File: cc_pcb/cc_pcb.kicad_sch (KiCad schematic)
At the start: 93 parts, among them J1 Conn_02x05_Odd_Even, J2 Micro_SD_Card_Det_Hirose_DM3AT, J3 4x4 Keypad, J4 DC-DC_JUMPER, J5 PS_WIRES, J6 PS_BJ, J7 DC-DC Converter, SW1 SW_Push, U1 ESP8266, U2 7in_display_controller, U3 RFID_Scanner, U4 TFT_2.8IN_DISPLAY, U5 74HC14, U6 STM32F091RCTx, U7 LD1117S33TR_SOT223, U8 TPS56325x, U9 4N28

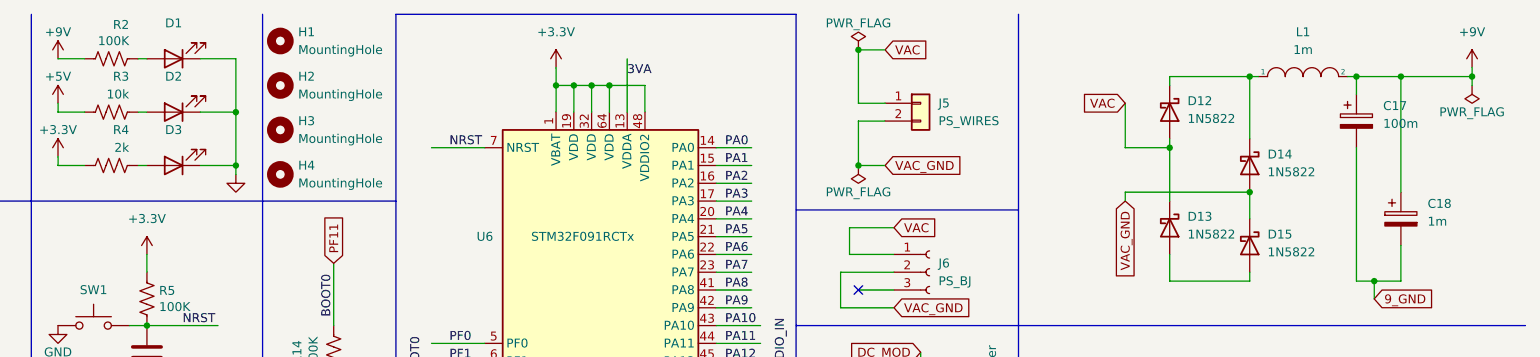
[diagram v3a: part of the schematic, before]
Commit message: 1:1 footprint changes and layout modded to follow rules
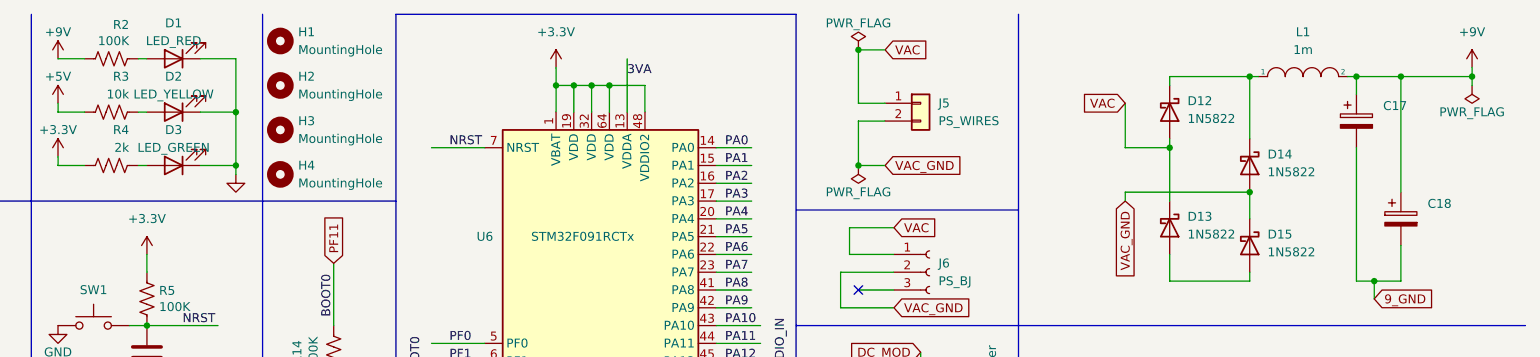
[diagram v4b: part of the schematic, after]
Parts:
- C17: value 100m -> (none); footprint Capacitor_THT:CP_Radial_D8.0mm_P3.50mm -> (none)
- C18: value 1m -> (none)
- D1: value (none) -> LED_RED
- D2: value (none) -> LED_YELLOW
- D3: value (none) -> LED_GREEN
- H1, H2: footprint (none) -> MountingHole:MountingHole_8.4mm_M8
- H5, H9: footprint (none) -> MountingHole:MountingHole_2.2mm_M2_ISO7380
- L2: footprint Inductor_THT:L_Radial_D7.5mm_P5.00mm_Fastron_07P -> (none)
- U2: footprint (none) -> imported_footprints:RA8875_TFT_Breakout
- U8: footprint (none) -> Package_TO_SOT_SMD:SOT-563
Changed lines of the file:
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@@
   (junction (at 74.93 146.05) (diameter 0) (color 0 0 0 0)
   )
-  (junction (at 147.32 184.15) (diameter 0) (color 0 0 0 0)
-  )
   (junction (at 262.89 100.33) (diameter 0) (color 0 0 0 0)
   )
@@
   (junction (at 135.89 156.21) (diameter 0) (color 0 0 0 0)
   )
+  (junction (at 147.32 184.15) (diameter 0) (color 0 0 0 0)
+  )
   (junction (at 215.9 154.94) (diameter 0) (color 0 0 0 0)
   )
@@
     (stroke (width 0) (type default) (color 0 0 0 0))
   )
-  (wire (pts (xy 147.32 184.15) (xy 154.94 184.15))
-    (stroke (width 0) (type default) (color 0 0 0 0))
-  )
   (wire (pts (xy 264.16 86.36) (xy 264.16 78.74))
     (stroke (width 0) (type default) (color 0 0 0 0))
@@
     (stroke (width 0) (type default) (color 0 0 0 0))
   )
+  (wire (pts (xy 147.32 184.15) (xy 154.94 184.15))
+    (stroke (width 0) (type default) (color 0 0 0 0))
+  )
   (wire (pts (xy 160.02 173.99) (xy 160.02 184.15))
     (stroke (width 0) (type default) (color 0 0 0 0))
@@
       (effects (font (size 1.27 1.27)) (justify left))
     )
-    (property "Footprint" "" (id 2) (at 106.68 22.86 0)
+    (property "Footprint" "MountingHole:MountingHole_8.4mm_M8" (id 2) (at 106.68 22.86 0)
       (effects (font (size 1.27 1.27)) hide)
     )
@@
       (effects (font (size 1.27 1.27)) (justify left))
     )
-    (property "Footprint" "" (id 2) (at 35.56 171.45 0)
+    (property "Footprint" "imported_footprints:RA8875_TFT_Breakout" (id 2) (at 35.56 171.45 0)
       (effects (font (size 1.27 1.27)) hide)
     )
@@
       (effects (font (size 1.27 1.27)) (justify left))
     )
-    (property "Footprint" "" (id 2) (at 182.88 77.47 0)
+    (property "Footprint" "MountingHole:MountingHole_2.2mm_M2_ISO7380" (id 2) (at 182.88 77.47 0)
       (effects (font (size 1.27 1.27)) hide)
     )
@@
     (property "Reference" "L2" (id 0) (at 271.78 77.47 0))
     (property "Value" "2.2uH" (id 1) (at 271.78 74.93 0))
-    (property "Footprint" "Inductor_THT:L_Radial_D7.5mm_P5.00mm_Fastron_07P" (id 2) (at 271.78 73.66 0)
+    (property "Footprint" "" (id 2) (at 271.78 73.66 0)
       (effects (font (size 1.27 1.27)) hide)
     )
@@
     (pin "1")
   )
-  (symbol (lib_id "power:+3.3V") (at 154.94 184.15 0) (unit 1)
-    (in_bom yes) (on_board yes) (fields_autoplaced)
-    (property "Reference" "#PWR024" (id 0) (at 154.94 187.96 0)
-      (effects (font (size 1.27 1.27)) hide)
-    )
-    (property "Value" "+3.3V" (id 1) (at 154.94 179.07 0))
-    (property "Footprint" "" (id 2) (at 154.94 184.15 0)
-      (effects (font (size 1.27 1.27)) hide)
-    )
-    (property "Datasheet" "" (id 3) (at 154.94 184.15 0)
-      (effects (font (size 1.27 1.27)) hide)
-    )
-    (pin "1")
-  )
   (symbol (lib_id "Mechanical:MountingHole") (at 15.24 125.73 0) (unit 1)
     (in_bom yes) (on_board yes) (fields_autoplaced)
@@
       (effects (font (size 1.27 1.27)) (justify left))
     )
-    (property "Footprint" "" (id 2) (at 15.24 125.73 0)
+    (property "Footprint" "MountingHole:MountingHole_2.2mm_M2_ISO7380" (id 2) (at 15.24 125.73 0)
       (effects (font (size 1.27 1.27)) hide)
     )
@@
       (effects (font (size 1.27 1.27)) (justify left))
     )
-    (property "Value" "100m" (id 1) (at 264.16 28.3209 0)
+    (property "Value" "" (id 1) (at 264.16 28.3209 0)
       (effects (font (size 1.27 1.27)) (justify left))
     )
-    (property "Footprint" "Capacitor_THT:CP_Radial_D8.0mm_P3.50mm" (id 2) (at 261.3152 31.75 0)
+    (property "Footprint" "" (id 2) (at 261.3152 31.75 0)
       (effects (font (size 1.27 1.27)) hide)
     )
@@
     (in_bom yes) (on_board yes)
     (property "Reference" "D1" (id 0) (at 91.44 13.97 0))
-    (property "Value" "" (id 1) (at 91.44 16.51 0))
+    (property "Value" "LED_RED" (id 1) (at 91.44 16.51 0))
     (property "Footprint" "LED_SMD:LED_0805_2012Metric_Pad1.15x1.40mm_HandSolder" (id 2) (at 91.44 19.05 0)
       (effects (font (size 1.27 1.27)) hide)
@@
     (in_bom yes) (on_board yes)
     (property "Reference" "D3" (id 0) (at 91.44 29.21 0))
-    (property "Value" "" (id 1) (at 91.44 31.75 0))
+    (property "Value" "LED_GREEN" (id 1) (at 91.44 31.75 0))
     (property "Footprint" "LED_SMD:LED_0805_2012Metric_Pad1.15x1.40mm_HandSolder" (id 2) (at 91.44 34.29 0)
       (effects (font (size 1.27 1.27)) hide)
@@
     (in_bom yes) (on_board yes)
     (property "Reference" "D2" (id 0) (at 91.44 21.59 0))
-    (property "Value" "" (id 1) (at 91.44 24.13 0))
+    (property "Value" "LED_YELLOW" (id 1) (at 91.44 24.13 0))
     (property "Footprint" "LED_SMD:LED_0805_2012Metric_Pad1.15x1.40mm_HandSolder" (id 2) (at 91.44 26.67 0)
       (effects (font (size 1.27 1.27)) hide)
@@
     (pin "2")
   )
+  (symbol (lib_id "power:+3.3V") (at 154.94 184.15 0) (unit 1)
+    (in_bom yes) (on_board yes) (fields_autoplaced)
+    (property "Reference" "#PWR0103" (id 0) (at 154.94 187.96 0)
+      (effects (font (size 1.27 1.27)) hide)
+    )
+    (property "Value" "+3.3V" (id 1) (at 154.94 179.07 0))
+    (property "Footprint" "" (id 2) (at 154.94 184.15 0)
+      (effects (font (size 1.27 1.27)) hide)
+    )
+    (property "Datasheet" "" (id 3) (at 154.94 184.15 0)
+      (effects (font (size 1.27 1.27)) hide)
+    )
+    (pin "1")
+  )
   (symbol (lib_id "power:+3.3V") (at 215.9 153.67 0) (unit 1)
     (in_bom yes) (on_board yes)
@@
       (effects (font (size 1.27 1.27)) (justify left))
     )
-    (property "Footprint" "" (id 2) (at 106.68 16.51 0)
+    (property "Footprint" "MountingHole:MountingHole_8.4mm_M8" (id 2) (at 106.68 16.51 0)
       (effects (font (size 1.27 1.27)) hide)
     )
@@
       (effects (font (size 1.27 1.27)) (justify left))
     )
-    (property "Value" "1m" (id 1) (at 270.51 42.2909 0)
+    (property "Value" "" (id 1) (at 270.51 42.2909 0)
       (effects (font (size 1.27 1.27)) (justify left))
     )
@@
     (property "Reference" "U8" (id 0) (at 251.46 66.04 0))
     (property "Value" "TPS56325x" (id 1) (at 251.46 68.58 0))
-    (property "Footprint" "" (id 2) (at 252.73 82.55 0)
+    (property "Footprint" "Package_TO_SOT_SMD:SOT-563" (id 2) (at 252.73 82.55 0)
       (effects (font (size 1.27 1.27)) (justify left) hide)
     )
@@
       (reference "#PWR023") (unit 1) (value "+3.3V") (footprint "")
     )
-    (path "/4178555d-085f-4746-8b73-252890ae63e8"
-      (reference "#PWR024") (unit 1) (value "+3.3V") (footprint "")
-    )
     (path "/e65bab67-68b7-4b22-a939-6f2c05164d2a"
       (reference "#PWR025") (unit 1) (value "GND") (footprint "")
@@
       (reference "#PWR0102") (unit 1) (value "+3.3V") (footprint "")
     )
+    (path "/ac5cf4af-2e8b-411c-ae77-44d668a99ac1"
+      (reference "#PWR0103") (unit 1) (value "+3.3V") (footprint "")
+    )
     (path "/1075c308-b5bb-44bc-847a-178364e5c8cd"
       (reference "C1") (unit 1) (value ".1uF") (footprint "Capacitor_SMD:C_0805_2012Metric_Pad1.18x1.45mm_HandSolder")
@@
     )
     (path "/794a597f-3512-43df-bd6b-427648e280ef"
-      (reference "C17") (unit 1) (value "100m") (footprint "Capacitor_THT:CP_Radial_D8.0mm_P3.50mm")
+      (reference "C17") (unit 1) (value "1m") (footprint "Capacitor_THT:CP_Radial_D12.5mm_P5.00mm")
     )
     (path "/d16102a1-071c-4c6a-bcbb-f75549c600e1"
-      (reference "C18") (unit 1) (value "1m") (footprint "Capacitor_THT:C_Radial_D18.0mm_H35.5mm_P7.50mm")
+      (reference "C18") (unit 1) (value "10m") (footprint "Capacitor_THT:C_Radial_D18.0mm_H35.5mm_P7.50mm")
     )
     (path "/fd6280ec-b253-4a2e-87f5-9c4044771c56"
@@
     )
     (path "/2cd518d6-3ac7-4c70-b904-23c3817bb90f"
-      (reference "L2") (unit 1) (value "2.2uH") (footprint "Inductor_THT:L_Radial_D7.5mm_P5.00mm_Fastron_07P")
+      (reference "L2") (unit 1) (value "2.2uH") (footprint "Inductor_SMD:L_0805_2012Metric_Pad1.15x1.40mm_HandSolder")
     )
     (path "/bca83724-6370-4365-831e-519f12b9ee70"

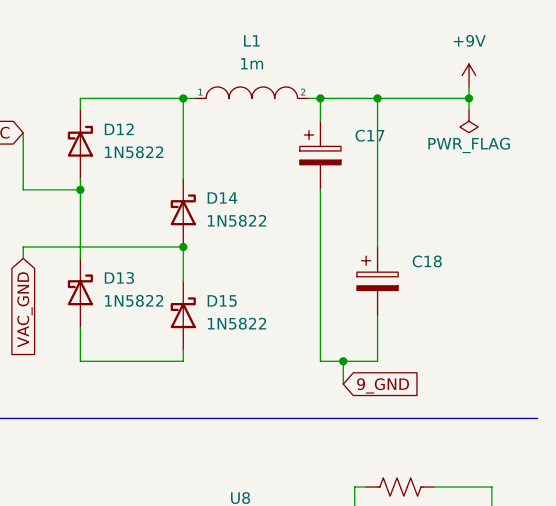
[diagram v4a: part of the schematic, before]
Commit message: updated schematic with text descriptions for each block. Also, added 0 ohm resistor and 10 ohm current limiting resistor to pcb. Minor changes were made to the designed buck converter circuit.
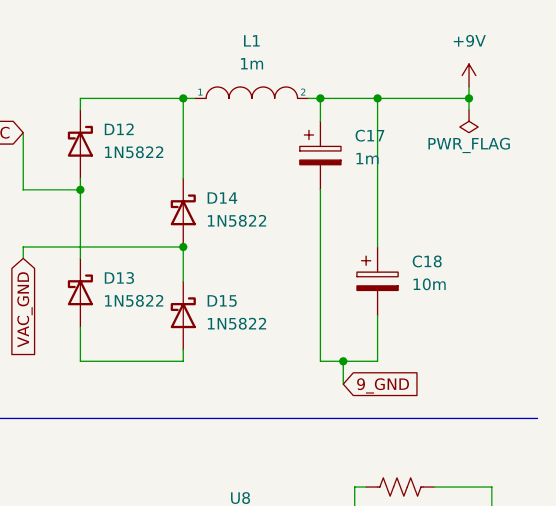
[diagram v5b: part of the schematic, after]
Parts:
- C17: value (none) -> 1m; footprint (none) -> Capacitor_THT:CP_Radial_D12.5mm_P5.00mm
- C18: value (none) -> 10m
- L2: footprint (none) -> Inductor_SMD:L_0805_2012Metric_Pad1.15x1.40mm_HandSolder
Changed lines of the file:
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@@
     (property "Reference" "L2" (id 0) (at 271.78 77.47 0))
     (property "Value" "2.2uH" (id 1) (at 271.78 74.93 0))
-    (property "Footprint" "" (id 2) (at 271.78 73.66 0)
+    (property "Footprint" "Inductor_SMD:L_0805_2012Metric_Pad1.15x1.40mm_HandSolder" (id 2) (at 271.78 73.66 0)
       (effects (font (size 1.27 1.27)) hide)
     )
@@
       (effects (font (size 1.27 1.27)) (justify left))
     )
-    (property "Value" "" (id 1) (at 264.16 28.3209 0)
-      (effects (font (size 1.27 1.27)) (justify left))
-    )
-    (property "Footprint" "" (id 2) (at 261.3152 31.75 0)
+    (property "Value" "1m" (id 1) (at 264.16 28.3209 0)
+      (effects (font (size 1.27 1.27)) (justify left))
+    )
+    (property "Footprint" "Capacitor_THT:CP_Radial_D12.5mm_P5.00mm" (id 2) (at 261.3152 31.75 0)
       (effects (font (size 1.27 1.27)) hide)
     )
@@
       (effects (font (size 1.27 1.27)) (justify left))
     )
-    (property "Value" "" (id 1) (at 270.51 42.2909 0)
-      (effects (font (size 1.27 1.27)) (justify left))
-    )
+    (property "Value" "10m" (id 1) (at 270.51 42.2909 0)
+      (effects (font (size 1.27 1.27)) (justify left))
+    )
